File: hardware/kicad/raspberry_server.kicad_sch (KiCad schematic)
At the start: 15 parts, among them J1 Door open, J2 Door GND, J6 Screw_Terminal_01x02, J7 Conn_01x04_Pin, J8 Screw_Terminal_01x04, Q1 BT138-600, U1 MOC3063M

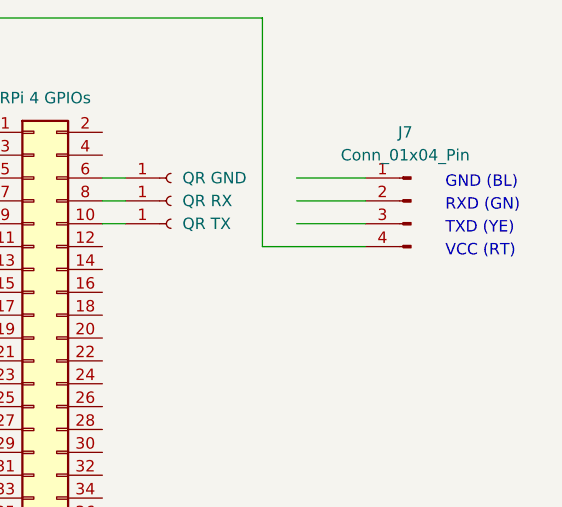
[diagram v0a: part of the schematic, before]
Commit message: latest tweaks; schematics now with QRCode part number & correct connector; QRCode Reading is working
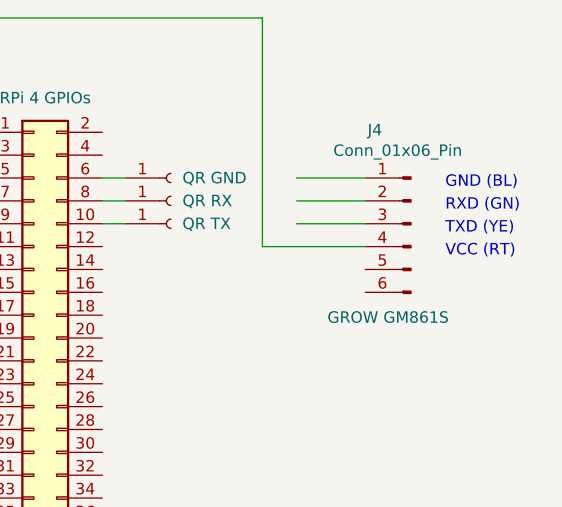
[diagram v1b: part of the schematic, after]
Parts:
- removed J7: Conn_01x04_Pin, symbol Connector:Conn_01x04_Pin
- added J4: Conn_01x06_Pin, symbol Connector:Conn_01x06_Pin
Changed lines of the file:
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@@
 	)
 	(symbol
-		(lib_id "Connector:Conn_01x04_Pin")
-		(at 240.03 83.82 0)
+		(lib_id "Connector:Conn_01x06_Pin")
+		(at 240.03 86.36 0)
 		(mirror y)
 		(unit 1)
@@
 		(on_board yes)
 		(dnp no)
-		(property "Reference" "J7"
-			(at 239.395 76.2 0)
+		(property "Reference" "J4"
+			(at 235.204 75.946 0)
 			(effects
 				(font
 					(size 1.27 1.27)
 				)
+				(justify right)
 			)
 		)
-		(property "Value" "Conn_01x04_Pin"
-			(at 239.395 78.74 0)
+		(property "Value" "Conn_01x06_Pin"
+			(at 231.394 78.232 0)
 			(effects
 				(font
 					(size 1.27 1.27)
 				)
+				(justify right)
 			)
 		)
 		(property "Footprint" ""
-			(at 240.03 83.82 0)
+			(at 240.03 86.36 0)
 			(effects
 				(font
@@
 		)
 		(property "Datasheet" "~"
-			(at 240.03 83.82 0)
+			(at 240.03 86.36 0)
 			(effects
 				(font
@@
 			)
 		)
-		(property "Description" ""
-			(at 240.03 83.82 0)
+		(property "Description" "Generic connector, single row, 01x06, script generated"
+			(at 240.03 86.36 0)
+			(effects
+				(font
+					(size 1.27 1.27)
+				)
+				(hide yes)
+			)
+		)
+		(property "Component" "GROW GM861S"
+			(at 237.49 96.774 0)
 			(effects
 				(font
@@
 			)
 		)
-		(pin "2"
+		(pin "6"
 		)
 		(pin "4"
@@
 		(pin "1"
 		)
+		(pin "5"
+		)
+		(pin "2"
+		)
 		(instances
-			(project "raspberry_server"
+			(project ""
 				(path "/0ac397e0-c0fd-4c9c-8284-d13288d36551"
-					(reference "J7")
+					(reference "J4")
 					(unit 1)
 				)
